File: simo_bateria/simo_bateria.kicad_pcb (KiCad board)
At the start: 2 copper layers, 66 x 35 mm, 14 parts, among them J1 BAT_LEVEL, J2 Plugin, J3 VBAT IN, J4 SWD, SW1 SW_Reed, U1 mod_mt3608, U2 BSS314PEH6327XTSA1

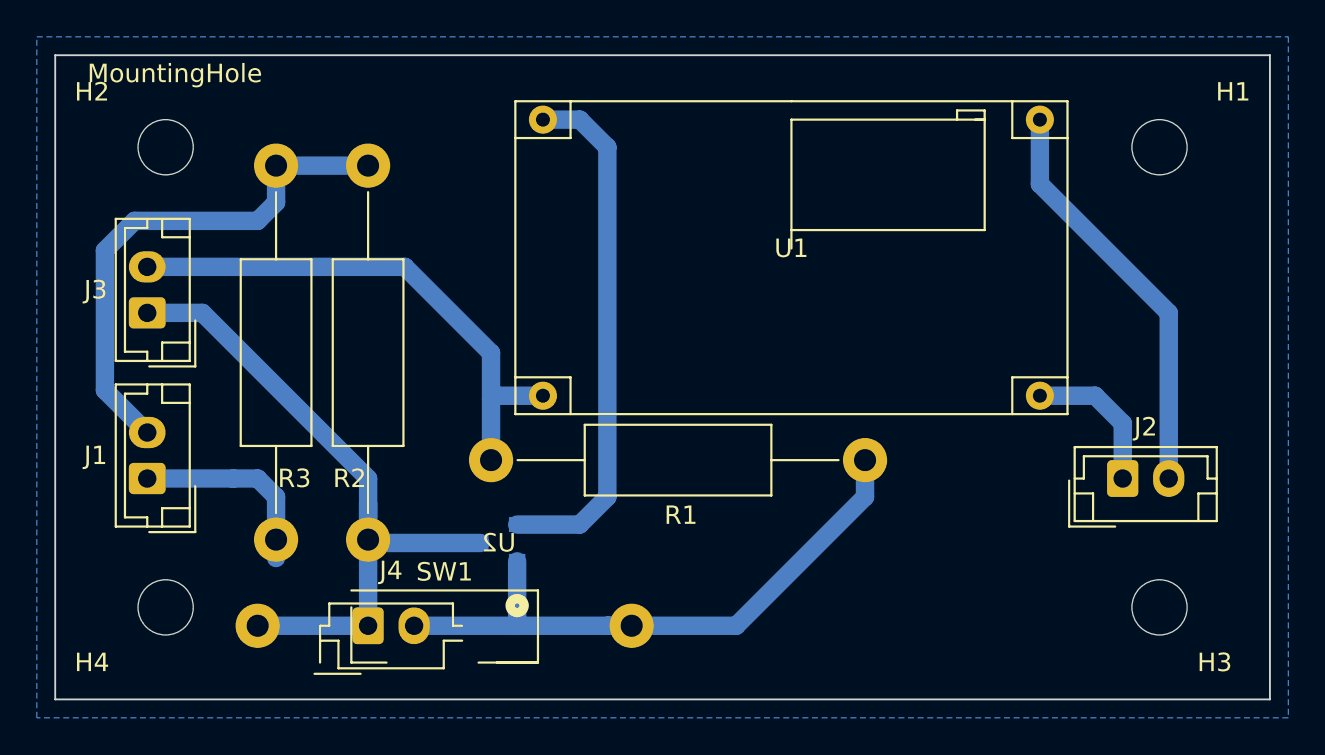
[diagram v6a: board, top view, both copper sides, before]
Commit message: [simo_bateria] Se elimino plano de tierra, faltaban archivos por actualizar
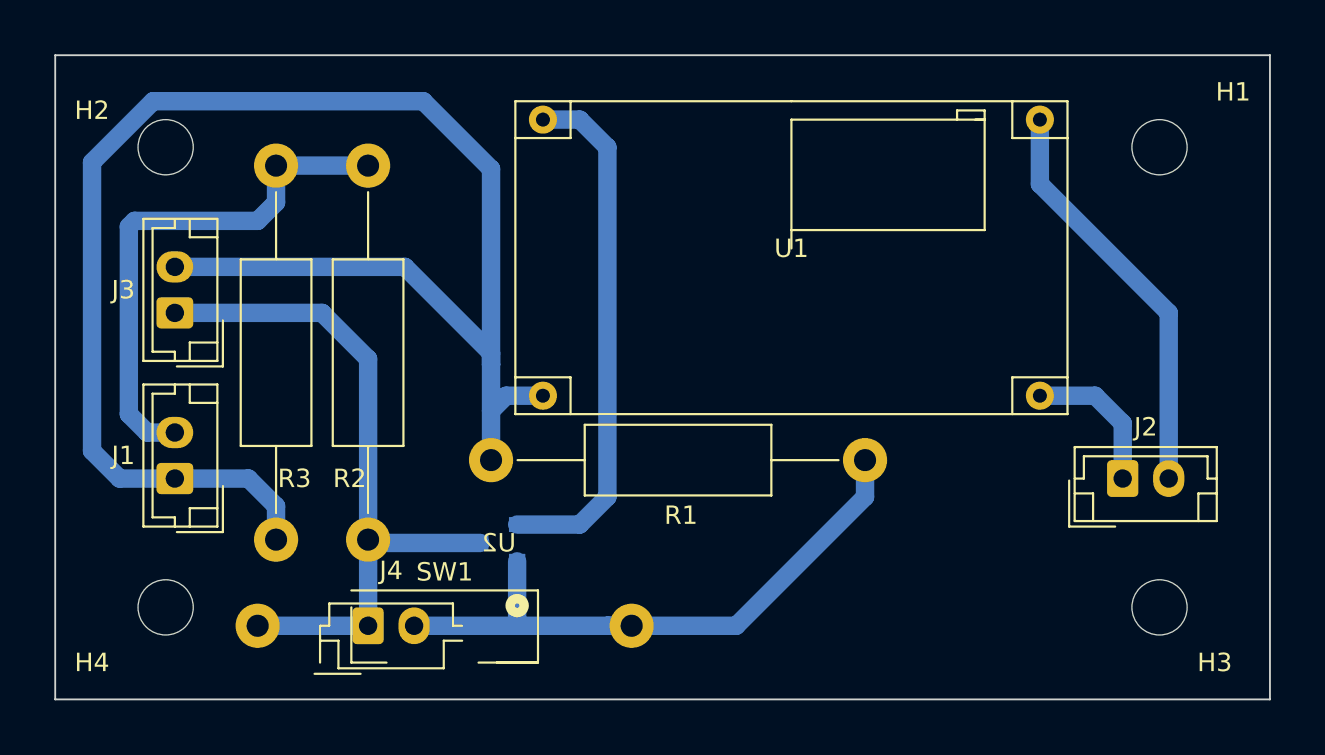
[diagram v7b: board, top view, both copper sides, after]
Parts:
- moved J1 1.50 mm to (161.5, 130.0)
- moved J3 1.50 mm to (161.5, 121.0)
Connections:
- J1 pad 1: Net-(J1-Pad1) -> GND
- J3 pad 2: Net-(J3-Pad2) -> GND
- R1 pad 2: Net-(J3-Pad2) -> GND
- R3 pad 2: Net-(J1-Pad1) -> GND
- U1 pad 2: Net-(J3-Pad2) -> GND
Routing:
- net GND: track 0.00 -> 92.1 mm
- net Net-(J3-Pad2): track 29.3 -> 0.00 mm
- net Net-(J1-Pad1): track 10.7 -> 0.00 mm
- net Net-(J3-Pad1): track 36.0 -> 37.5 mm
- removed copper zone on B.Cu, net (none)
